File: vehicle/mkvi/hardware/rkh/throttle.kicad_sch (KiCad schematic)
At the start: 6 parts, among them J701 Automotive_M.2, U701 TMUX1247DCKR, U702 TMUX1247DCKR

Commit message: m.2 connectors
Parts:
- J701: symbol formula:Automotive_M.2 -> OEM:Automotive_M.2
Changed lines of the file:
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@@
     (pin "1")
   )
-  (symbol (lib_id "formula:Automotive_M.2") (at 149.86 92.71 0) (unit 1)
+  (symbol (lib_id "OEM:Automotive_M.2") (at 149.86 92.71 0) (unit 1)
     (in_bom yes) (on_board yes) (fields_autoplaced)
     (property "Reference" "J701" (id 0) (at 149.86 43.815 0)

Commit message: caps
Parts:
- C701, C702: symbol formula:C_1uF -> OEM:1uF
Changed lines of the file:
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@@
     (pin "1")
   )
-  (symbol (lib_id "formula:C_1uF") (at 53.34 57.15 0) (unit 1)
+  (symbol (lib_id "OEM:1uF") (at 53.34 57.15 0) (unit 1)
     (in_bom yes) (on_board yes) (fields_autoplaced)
     (property "Reference" "C702" (id 0) (at 57.15 54.6099 0)
@@
     (pin "1")
   )
-  (symbol (lib_id "formula:C_1uF") (at 38.1 57.15 0) (unit 1)
+  (symbol (lib_id "OEM:1uF") (at 38.1 57.15 0) (unit 1)
     (in_bom yes) (on_board yes) (fields_autoplaced)
     (property "Reference" "C701" (id 0) (at 41.91 54.6099 0)

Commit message: resistors
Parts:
- removed RV701: R_Potentiometer_Dual, footprints:PTV1124420AA503, symbol Device:R_Potentiometer_Dual
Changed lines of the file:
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@@
     (pin "2")
-  )
-  (symbol (lib_id "Device:R_Potentiometer_Dual") (at 38.1 165.1 270) (unit 1)
-    (in_bom yes) (on_board yes)
-    (property "Reference" "RV701" (id 0) (at 39.37 176.53 90))
-    (property "Value" "R_Potentiometer_Dual" (id 1) (at 52.07 149.86 90))
-    (property "Footprint" "footprints:PTV1124420AA503" (id 2) (at 36.195 171.45 0)
-      (effects (font (size 1.27 1.27)) hide)
-    )
-    (property "Datasheet" "~" (id 3) (at 36.195 171.45 0)
-      (effects (font (size 1.27 1.27)) hide)
-    )
-    (pin "1")
-    (pin "2")
-    (pin "3")
-    (pin "4")
-    (pin "5")
-    (pin "6")
   )
   (symbol (lib_id "formula:TMUX1247DCKR") (at 49.53 127 0) (unit 1)

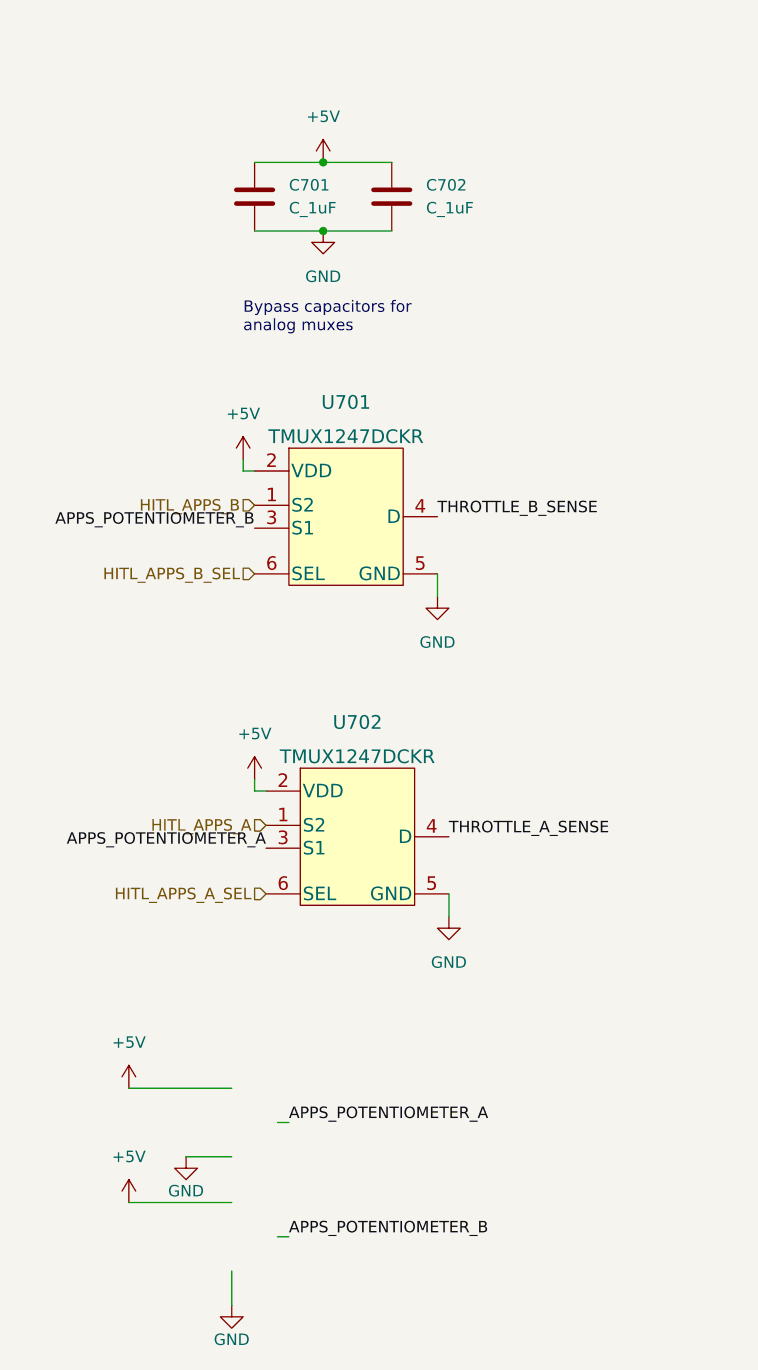
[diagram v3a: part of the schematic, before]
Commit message: update boards from library, fix issues that arose
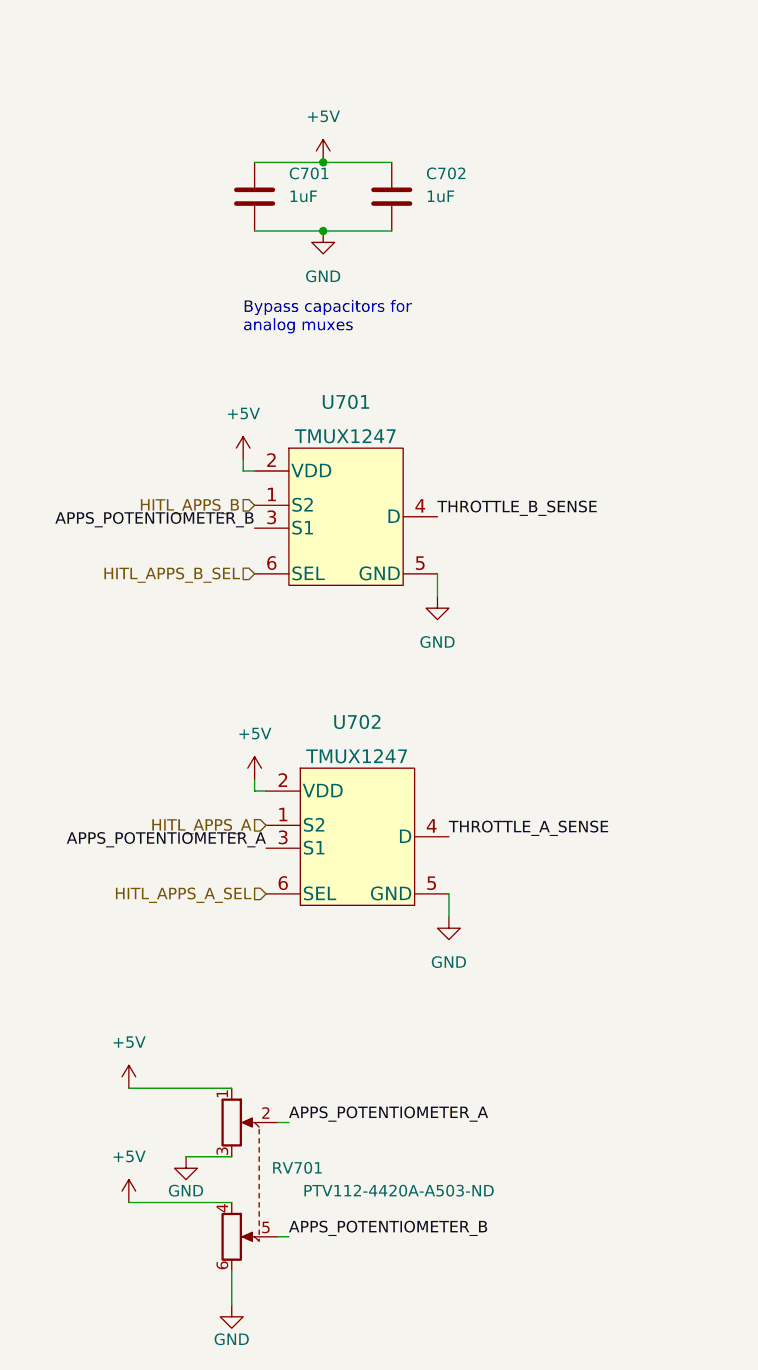
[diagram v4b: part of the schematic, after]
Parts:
- added RV701: PTV112-4420A-A503-ND, footprints:PTV1124420AA503, symbol OEM:PTV112-4420A-A503-ND
- C701, C702: value C_1uF -> 1uF; footprint footprints:C_0603_1608Metric -> OEM:C_0603; DKPN (none) -> 1276-1184-2-ND; MFN DK -> Samsung Electro-Mechanics; MPN 1276-6470-1-ND -> CL10B105KA8NNNC; NewDesigns (none) -> YES; Package (none) -> 0603; PurchasingLink https://www.digikey.com/en/products/detail/samsung-electro-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 -> (none); Stocked (none) -> Reel; Style (none) -> SMD
- J701: DKPN (none) -> MOUSER:945-CNU027S0672001VE; MFN (none) -> Yamaichi Electronics; MPN (none) -> CNU027S-067-2001-VE; NewDesigns (none) -> YES; Package (none) -> Custom; Stocked (none) -> Tape; Style (none) -> SMD
- U701, U702: value TMUX1247DCKR -> TMUX1247; symbol formula:TMUX1247DCKR -> OEM:TMUX1247; DKPN (none) -> 296-TMUX1247DCKRDKR-ND; MFN (none) -> Texas Instruments; MPN (none) -> TMUX1247DCKR; NewDesigns (none) -> YES; Package (none) -> SC70; Stocked (none) -> Digi-Reel; Style (none) -> THT
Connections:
- net +5V: now also RV701.1, RV701.4
- net APPS_POTENTIOMETER_A: now also RV701.2
- net APPS_POTENTIOMETER_B: now also RV701.5
- net GND: now also RV701.3, RV701.6
